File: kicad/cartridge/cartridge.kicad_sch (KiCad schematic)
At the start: 11 parts, among them J1 Card edge (87715-9106 mate), U1 ATF22V10C-10PU, U2 AT28C256-15PU, U3 AT28C256-15PU, U4 AS7C256C-15PCN, U5 AS7C256C-15PCN

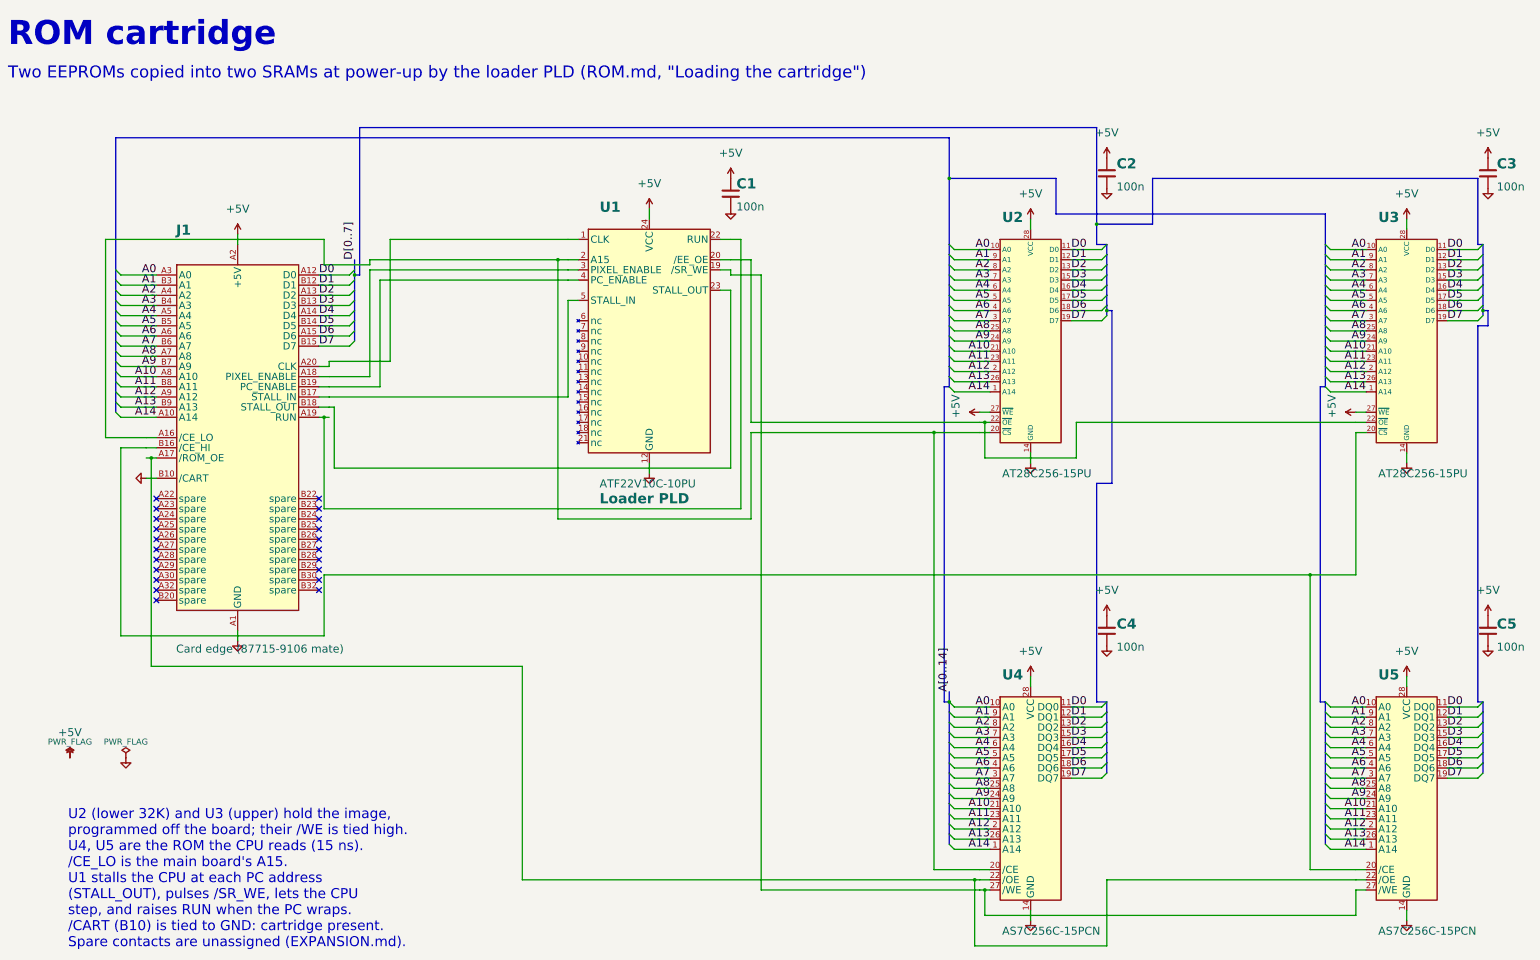
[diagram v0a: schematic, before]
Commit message: Tidy every schematic sheet: spread parts, straight runs, buses kept, horizontal tabs
Shared port, expansion and cartridge sheets laid out by hand; buses from
other sheets get a bus label at each chip, busy control nets a label at
each pin; some PLD and connector symbols reordered so wires run straight;
sideways power symbols read across. 0 netlist problems, no overlaps.

Co-Authored-By: Claude Opus 5.5 (1M context) <noreply@anthropic.com>
Claude-Session: https://claude.ai/code/session_01L9AkLuEg13EebxDmgXsaEp
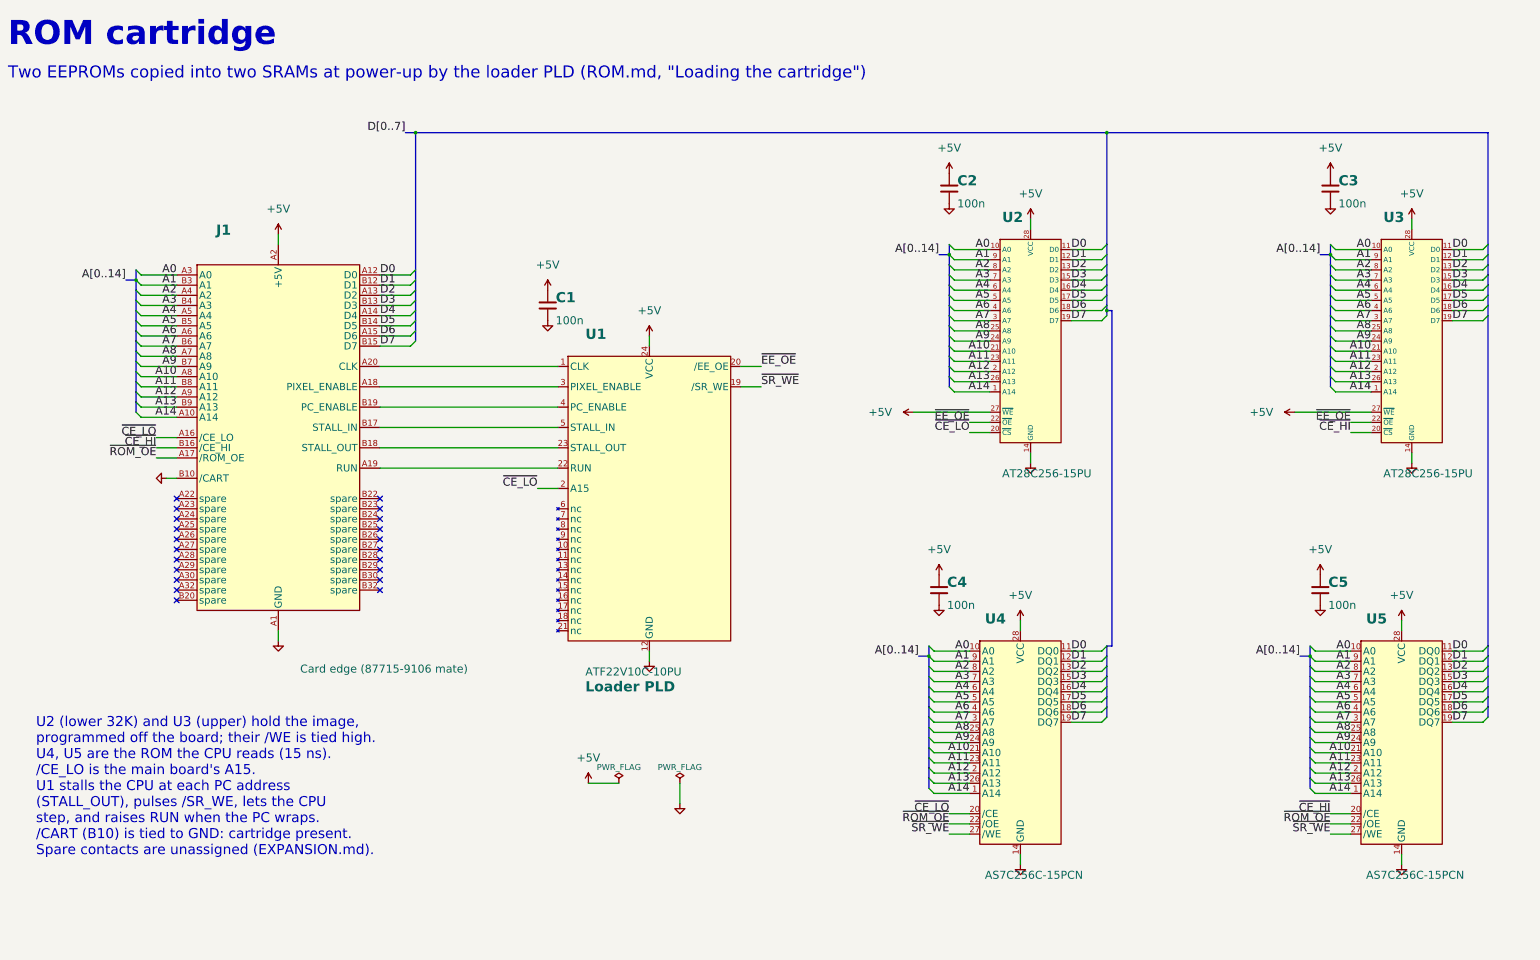
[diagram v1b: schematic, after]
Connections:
- net ~{CE_LO}: now reaches J1.A16 (/CE_LO), U1.2 (A15), U2.20 (~{CS}), U4.20 (/CE)
- net ~{EE_OE}: now reaches U1.20 (/EE_OE), U2.22 (~{OE}), U3.22 (~{OE})
- net ~{ROM_OE}: now reaches J1.A17 (/ROM_OE), U4.22 (/OE), U5.22 (/OE)
- net ~{CE_HI}: now reaches J1.B16 (/CE_HI), U3.20 (~{CS}), U5.20 (/CE)
- net ~{SR_WE}: now reaches U1.19 (/SR_WE), U4.27 (/WE), U5.27 (/WE)
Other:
- moved on the sheet: J1

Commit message: Cartridge: JP1 solder jumper for a 32K or 64K ROM
The upper EEPROM/SRAM pair's /CE (/CE_UP) comes from JP1: bridged 1-2
(as made) to GND, so a 32K cart with U3 and U5 only answers in both
halves; cut and bridged 2-3 to /CE_HI for 64K with U2 and U4 fitted.

Co-Authored-By: Claude Opus 5.5 (1M context) <noreply@anthropic.com>
Claude-Session: https://claude.ai/code/session_01PNJoPfzmo1tu8EorCrua96
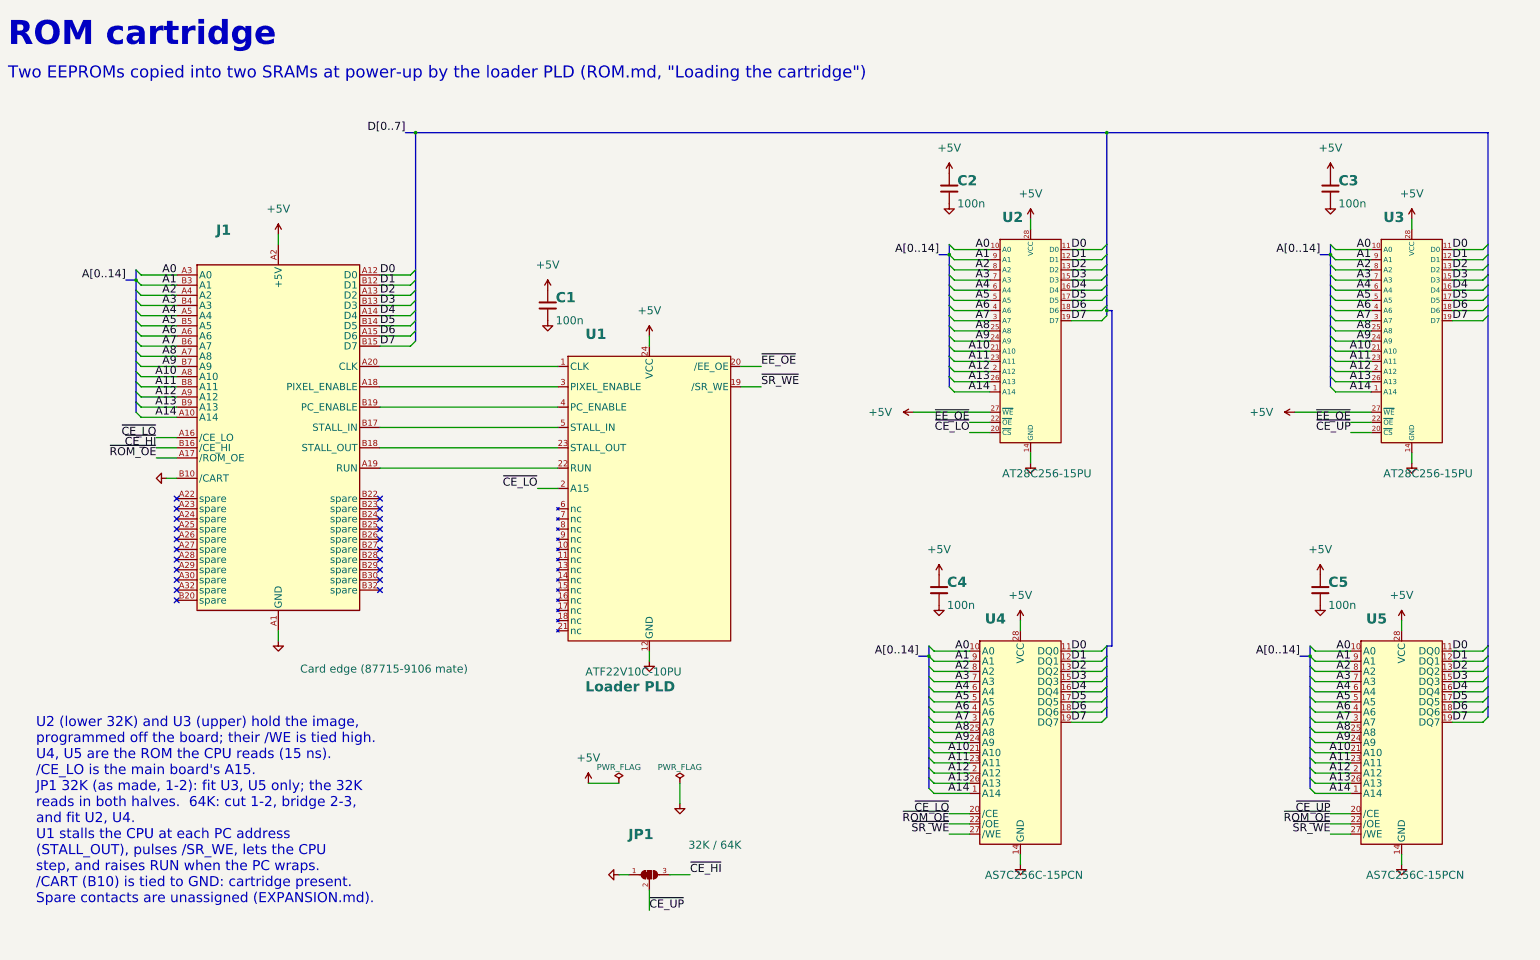
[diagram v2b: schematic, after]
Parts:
- added JP1: 32K / 64K, Jumper:SolderJumper-3_P1.3mm_Bridged12_RoundedPad1.0x1.5mm_NumberLabels, symbol Jumper:SolderJumper_3_Bridged12
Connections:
- net GND: now also JP1.1 (A)
- net ~{CE_HI}: now also JP1.3 (B); no longer U3.20 (~{CS}), U5.20 (/CE)
- new net ~{CE_UP}: JP1.2 (C), U3.20 (~{CS}), U5.20 (/CE)
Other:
- note added: "JP1 32K (as made, 1-2): fit U3, U5 only; the 32K"
- note added: "and fit U2, U4."
- note added: "reads in both halves. 64K: cut 1-2, bridge 2-3,"
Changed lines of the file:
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@@
   (symbol (lib_id "power:GND") (at 342.9 161.29 0) (unit 1) (in_bom yes) (on_board yes) (dnp no) (property "Reference" "#PWR0129" (at 342.9 161.29 0) (effects (font (size 1.27 1.27)) hide)) (property "Value" "GND" (at 342.9 167.64 0) (effects (font (size 2 2)) hide)) (property "Footprint" "" (at 342.9 161.29 0) (effects (font (size 1.27 1.27)) hide)) (property "Datasheet" "" (at 342.9 161.29 0) (effects (font (size 1.27 1.27)) hide)) (pin "1") (instances (project "cartridge" (path "/58e6aaf0-b096-58ec-a49b-041f90960c95" (reference "#PWR0129") (unit 1)))))
   (symbol (lib_id "placard_std:C") (at 342.9 157.48 0) (unit 1) (in_bom yes) (on_board yes) (dnp no) (property "Reference" "C5" (at 344.9 156.98 0) (effects (font (size 2.54 2.54) bold) (justify left bottom))) (property "Value" "100n" (at 344.9 160.08 0) (effects (font (size 2 2)) (justify left top))) (property "Footprint" "Capacitor_THT:C_Disc_D5.0mm_W2.5mm_P5.00mm" (at 342.9 157.48 0) (effects (font (size 1.27 1.27)) hide)) (property "Datasheet" "~" (at 342.9 157.48 0) (effects (font (size 1.27 1.27)) hide)) (pin "1") (pin "2") (instances (project "cartridge" (path "/58e6aaf0-b096-58ec-a49b-041f90960c95" (reference "C5") (unit 1)))))
+  (wire (pts (xy 170.18 228.6) (xy 167.64 228.6)) (stroke (width 0) (type default)))
+  (symbol (lib_id "power:GND") (at 167.64 228.6 270) (unit 1) (in_bom yes) (on_board yes) (dnp no) (property "Reference" "#PWR0130" (at 167.64 228.6 0) (effects (font (size 1.27 1.27)) hide)) (property "Value" "GND" (at 159.29 228.6 90) (effects (font (size 2 2)) hide)) (property "Footprint" "" (at 167.64 228.6 0) (effects (font (size 1.27 1.27)) hide)) (property "Datasheet" "" (at 167.64 228.6 0) (effects (font (size 1.27 1.27)) hide)) (pin "1") (instances (project "cartridge" (path "/58e6aaf0-b096-58ec-a49b-041f90960c95" (reference "#PWR0130") (unit 1)))))
+  (symbol (lib_id "Jumper:SolderJumper_3_Bridged12") (at 175.26 228.6 0) (unit 1) (in_bom yes) (on_board yes) (dnp no) (property "Reference" "JP1" (at 170 220 0) (effects (font (size 2.54 2.54) bold) (justify left bottom))) (property "Value" "32K / 64K" (at 185 220 0) (effects (font (size 2 2)) (justify left top))) (property "Footprint" "Jumper:SolderJumper-3_P1.3mm_Bridged12_RoundedPad1.0x1.5mm_NumberLabels" (at 175.26 228.6 0) (effects (font (size 1.27 1.27)) hide)) (property "Datasheet" "~" (at 175.26 228.6 0) (effects (font (size 1.27 1.27)) hide)) (pin "1") (pin "2") (pin "3") (instances (project "cartridge" (path "/58e6aaf0-b096-58ec-a49b-041f90960c95" (reference "JP1") (unit 1)))))
   (text "U2 (lower 32K) and U3 (upper) hold the image," (at 22 192 0) (effects (font (size 2.5 2.5)) (justify left bottom)))
   (text "programmed off the board; their /WE is tied high." (at 22 196 0) (effects (font (size 2.5 2.5)) (justify left bottom)))
   (text "U4, U5 are the ROM the CPU reads (15 ns)." (at 22 200 0) (effects (font (size 2.5 2.5)) (justify left bottom)))
   (text "/CE_LO is the main board's A15." (at 22 204 0) (effects (font (size 2.5 2.5)) (justify left bottom)))
-  (text "U1 stalls the CPU at each PC address" (at 22 208 0) (effects (font (size 2.5 2.5)) (justify left bottom)))
-  (text "(STALL_OUT), pulses /SR_WE, lets the CPU" (at 22 212 0) (effects (font (size 2.5 2.5)) (justify left bottom)))
-  (text "step, and raises RUN when the PC wraps." (at 22 216 0) (effects (font (size 2.5 2.5)) (justify left bottom)))
-  (text "/CART (B10) is tied to GND: cartridge present." (at 22 220 0) (effects (font (size 2.5 2.5)) (justify left bottom)))
-  (text "Spare contacts are unassigned (EXPANSION.md)." (at 22 224 0) (effects (font (size 2.5 2.5)) (justify left bottom)))
+  (text "JP1 32K (as made, 1-2): fit U3, U5 only; the 32K" (at 22 208 0) (effects (font (size 2.5 2.5)) (justify left bottom)))
+  (text "reads in both halves.  64K: cut 1-2, bridge 2-3," (at 22 212 0) (effects (font (size 2.5 2.5)) (justify left bottom)))
+  (text "and fit U2, U4." (at 22 216 0) (effects (font (size 2.5 2.5)) (justify left bottom)))
+  (text "U1 stalls the CPU at each PC address" (at 22 220 0) (effects (font (size 2.5 2.5)) (justify left bottom)))
+  (text "(STALL_OUT), pulses /SR_WE, lets the CPU" (at 22 224 0) (effects (font (size 2.5 2.5)) (justify left bottom)))
+  (text "step, and raises RUN when the PC wraps." (at 22 228 0) (effects (font (size 2.5 2.5)) (justify left bottom)))
+  (text "/CART (B10) is tied to GND: cartridge present." (at 22 232 0) (effects (font (size 2.5 2.5)) (justify left bottom)))
+  (text "Spare contacts are unassigned (EXPANSION.md)." (at 22 236 0) (effects (font (size 2.5 2.5)) (justify left bottom)))
   (wire (pts (xy 57.15 78.74) (xy 48.26 78.74)) (stroke (width 0) (type default)))
   (label "A0" (at 57.15 78.74 180) (fields_autoplaced) (effects (font (size 2 2)) (justify right bottom)))
@@
   (bus (pts (xy 384.81 184.15) (xy 384.81 186.69)) (stroke (width 0) (type default)))
   (bus (pts (xy 384.81 186.69) (xy 384.81 189.23)) (stroke (width 0) (type default)))
+  (wire (pts (xy 175.26 232.41) (xy 175.26 237.49)) (stroke (width 0) (type default)))
+  (label "~{CE_UP}" (at 175.26 237.49 0) (fields_autoplaced) (effects (font (size 2 2)) (justify left bottom)))
+  (wire (pts (xy 180.34 228.6) (xy 185.42 228.6)) (stroke (width 0) (type default)))
+  (label "~{CE_HI}" (at 185.42 228.6 0) (fields_autoplaced) (effects (font (size 2 2)) (justify left bottom)))
   (label "~{CE_LO}" (at 52.07 119.38 180) (fields_autoplaced) (effects (font (size 2 2)) (justify right bottom)))
   (label "~{CE_HI}" (at 52.07 121.92 180) (fields_autoplaced) (effects (font (size 2 2)) (justify right bottom)))
@@
   (label "~{CE_LO}" (at 255.27 118.11 180) (fields_autoplaced) (effects (font (size 2 2)) (justify right bottom)))
   (label "~{EE_OE}" (at 255.27 115.57 180) (fields_autoplaced) (effects (font (size 2 2)) (justify right bottom)))
-  (label "~{CE_HI}" (at 350.52 118.11 180) (fields_autoplaced) (effects (font (size 2 2)) (justify right bottom)))
+  (label "~{CE_UP}" (at 350.52 118.11 180) (fields_autoplaced) (effects (font (size 2 2)) (justify right bottom)))
   (label "~{EE_OE}" (at 350.52 115.57 180) (fields_autoplaced) (effects (font (size 2 2)) (justify right bottom)))
   (label "~{CE_LO}" (at 250.19 213.36 180) (fields_autoplaced) (effects (font (size 2 2)) (justify right bottom)))
   (label "~{ROM_OE}" (at 250.19 215.9 180) (fields_autoplaced) (effects (font (size 2 2)) (justify right bottom)))
   (label "~{SR_WE}" (at 250.19 218.44 180) (fields_autoplaced) (effects (font (size 2 2)) (justify right bottom)))
-  (label "~{CE_HI}" (at 345.44 213.36 180) (fields_autoplaced) (effects (font (size 2 2)) (justify right bottom)))
+  (label "~{CE_UP}" (at 345.44 213.36 180) (fields_autoplaced) (effects (font (size 2 2)) (justify right bottom)))
   (label "~{ROM_OE}" (at 345.44 215.9 180) (fields_autoplaced) (effects (font (size 2 2)) (justify right bottom)))
   (label "~{SR_WE}" (at 345.44 218.44 180) (fields_autoplaced) (effects (font (size 2 2)) (justify right bottom)))
